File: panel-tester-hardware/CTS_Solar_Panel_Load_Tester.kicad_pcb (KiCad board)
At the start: 2 copper layers, 57 x 67.5 mm, 18 parts, among them J1 Screw_Terminal_01x02, J2 Conn_01x02_Pin, J3 Conn_01x07, J4 Conn_01x03, U1 INA219AxD, U2 YAAJ_BluePill

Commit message: Add files via upload
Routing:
- net MCU_I2C_SCL: track 67.3 -> 40.6 mm
- net MCU_I2C_SDA: track 63.3 -> 70.3 mm
- net V_SOLAR_INPUT_POS: track 80.2 -> 84.2 mm

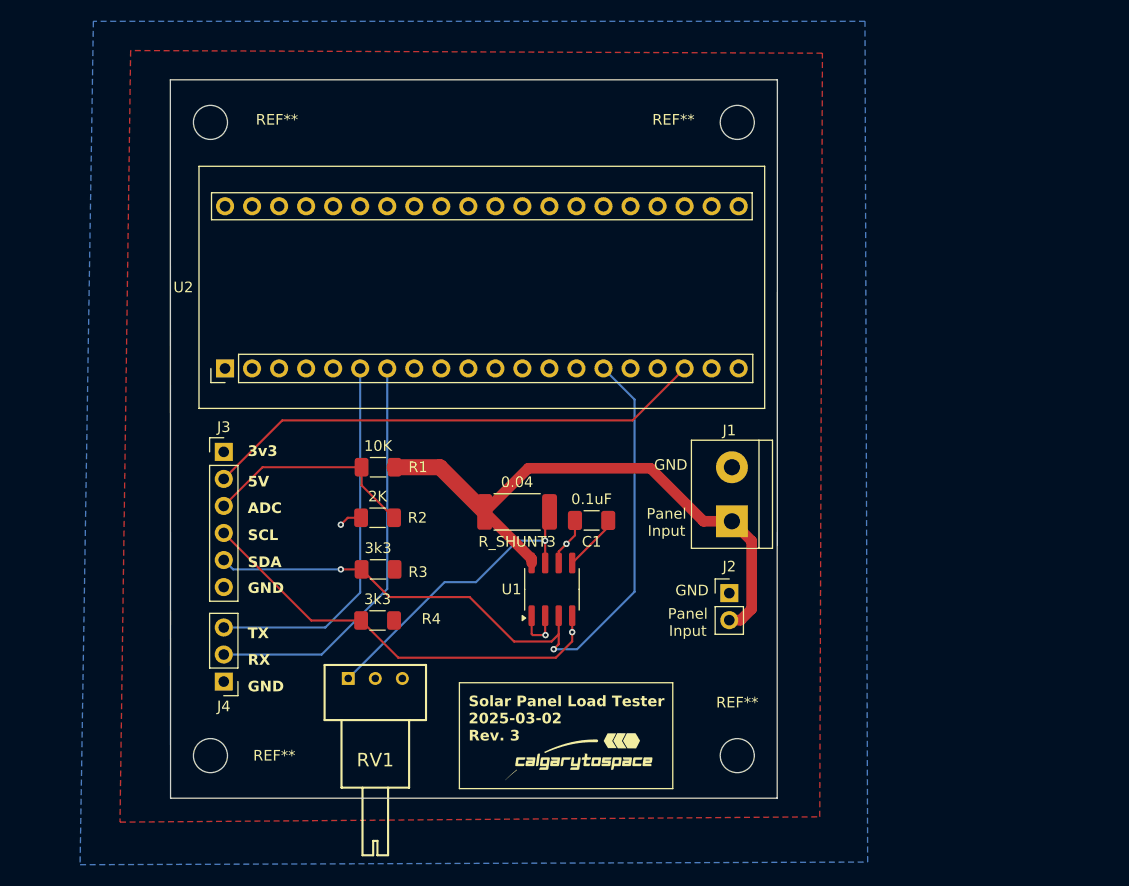
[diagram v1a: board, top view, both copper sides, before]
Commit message: made schematic for the amplifier and MOSFET
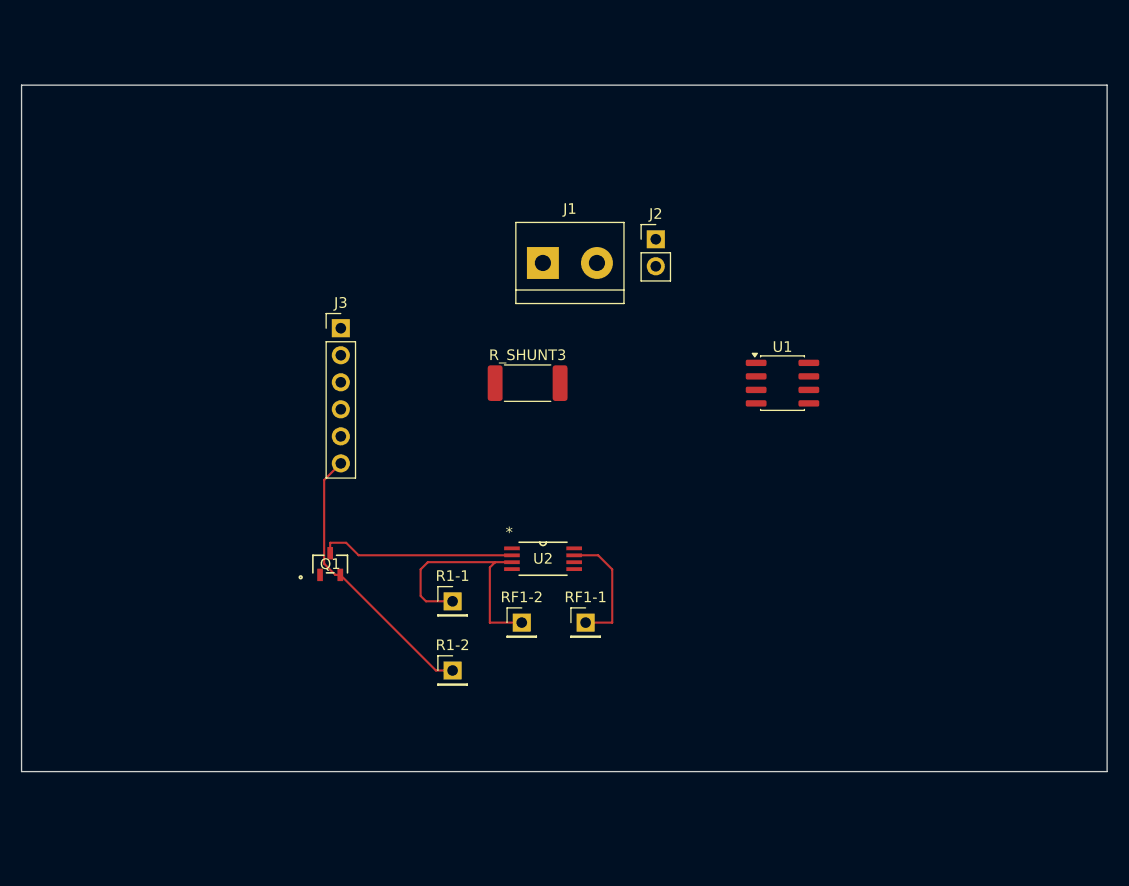
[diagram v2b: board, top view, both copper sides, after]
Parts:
- removed C1: 0.1uF, Capacitor_SMD:C_1206_3216Metric_Pad1.33x1.80mm_HandSolder
- removed G***: LOGO, LOGO
- removed J4: Conn_01x03, Connector_PinHeader_2.54mm:PinHeader_1x03_P2.54mm_Vertical
- removed R1: 10K, Resistor_SMD:R_1206_3216Metric_Pad1.30x1.75mm_HandSolder
- removed R2: 2K, Resistor_SMD:R_1206_3216Metric_Pad1.30x1.75mm_HandSolder
- removed R3, R4: 3k3, Resistor_SMD:R_1206_3216Metric_Pad1.30x1.75mm_HandSolder
- removed REF** (x4): MountingHole_3.2mm_M3, MountingHole:MountingHole_3.2mm_M3
- removed RV1: R_Potentiometer, PotentiometerCustom:3310C101102L
- added Q1: ~, mosfet:TO-236AB_SOT23_NEX, F.Cu at (107.0, 98.5)
- added R1-1: ~, Connector_PinHeader_2.54mm:PinHeader_1x01_P2.54mm_Vertical, F.Cu at (118.5, 102.0)
- added R1-2: ~, Connector_PinHeader_2.54mm:PinHeader_1x01_P2.54mm_Vertical, F.Cu at (118.5, 108.5)
- added RF1-1: ~, Connector_PinHeader_2.54mm:PinHeader_1x01_P2.54mm_Vertical, F.Cu at (131.0, 104.0)
- added RF1-2: ~, Connector_PinHeader_2.54mm:PinHeader_1x01_P2.54mm_Vertical, F.Cu at (125.0, 104.0)
- U2: value YAAJ_BluePill -> LM311PW; footprint BluePill:YAAJ_BluePill_2 -> lm311-footprints:PW8
- moved U2 34.8 mm to (127.0, 98.0), turned to 0 degrees
- moved J2 34.0 mm to (137.6, 68.0)
- moved J1 30.1 mm to (127.0, 70.2), turned to 0 degrees
- moved U1 29.1 mm to (149.5, 81.5), turned to 0 degrees
- moved J3 16.0 mm to (108.0, 76.3)
- moved R_SHUNT3 12.1 mm to (125.5, 81.5)
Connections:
- R_SHUNT3 pad 2: V_SOLAR_INPUT_POS -> Net-(U1-IN-)
- U1 pad 7: V_SOLAR_INPUT_POS -> Net-(U1-IN-)
- U2 pad 2: unconnected-(U2-PB13-Pad2) -> Net-(Q1-D)
- U2 pad 3: unconnected-(U2-PB14-Pad3) -> Net-(R1-1-Pin_1)
- U2 pad 6: Net-(J4-Pin_3) -> unconnected-(U2-BAL/STRB-Pad6)
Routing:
- net V_SOLAR_INPUT_POS: track 84.2 -> 0.00 mm, vias 1 -> 0
- net MCU_I2C_SDA: track 70.3 -> 0.00 mm, vias 2 -> 0
- net +5V: track 47.6 -> 0.00 mm
- net MCU_I2C_SCL: track 40.6 -> 0.00 mm, vias 1 -> 0
- net Net-(J4-Pin_3): track 35.2 -> 0.00 mm
- net Net-(RF1-1-Pin_1): track 38.6 -> 11.6 mm
- net Net-(R1-1-Pin_1): track 0.00 -> 23.4 mm
- net MCU_ADC_SENSE: track 20.5 -> 0.00 mm
- net Net-(Q1-D): track 0.00 -> 18.5 mm
- net GND: track 11.6 -> 26.3 mm, vias 3 -> 0
- net +3V3: track 5.40 -> 0.00 mm
- removed copper zone on F.Cu, net +3V3
- removed copper zone on B.Cu, net GND
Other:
- board size 57 x 67.5 mm -> 102 x 64.5 mm
- board text removed: "3v3"
- board text removed: "5V"
- board text removed: "ADC"
- board text removed: "GND"
- board text removed: "Panel Input"
- board text removed: "R4"
- board text removed: "RX"
- board text removed: "SCL"
- board text removed: "SDA"
- board text removed: "Solar Panel Load Tester 2025-03-02 Rev. 3"
- board text removed: "TX"

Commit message: fixed footprints and added headers
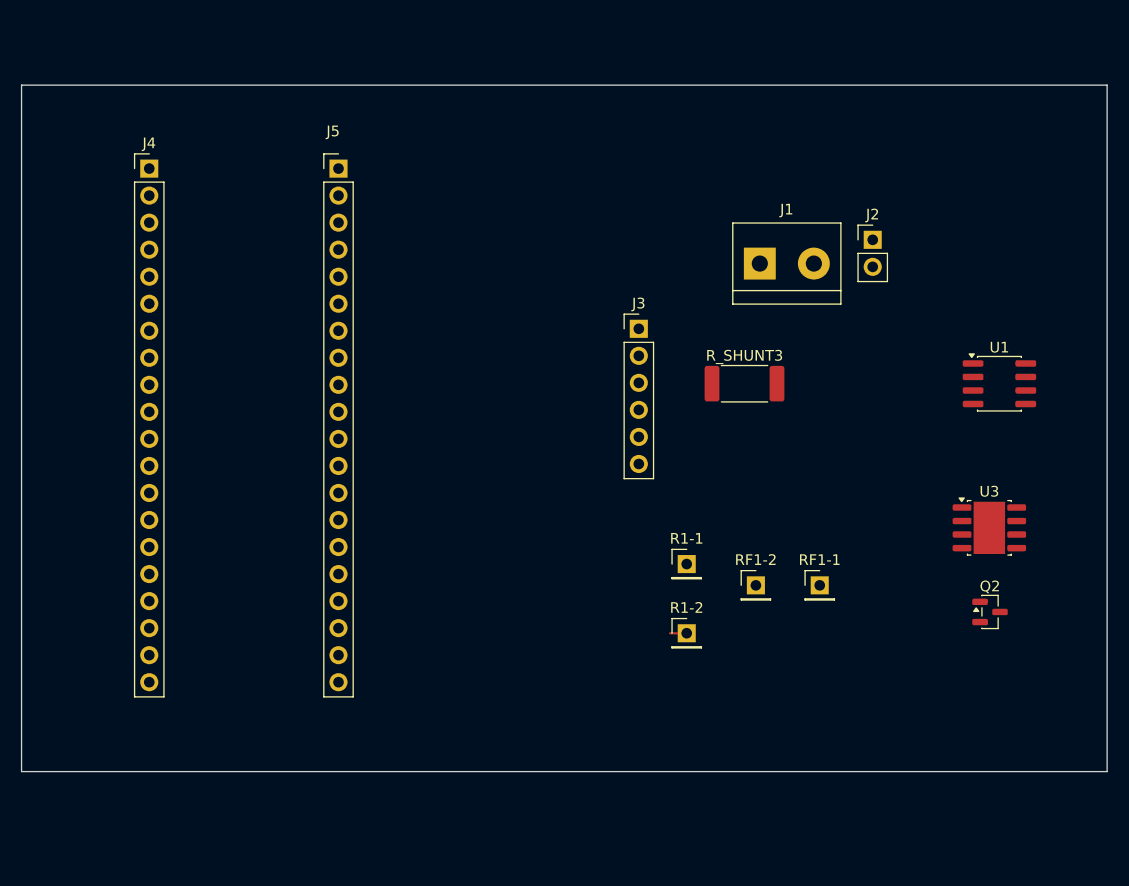
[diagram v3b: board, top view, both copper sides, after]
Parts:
- removed Q1: ~, mosfet:TO-236AB_SOT23_NEX
- removed U2: LM311PW, lm311-footprints:PW8
- added J4: Conn_01x20_Pin, Connector_PinHeader_2.54mm:PinHeader_1x20_P2.54mm_Vertical, F.Cu at (90.0, 61.3)
- added J5: Conn_01x20_Pin, Connector_PinHeader_2.54mm:PinHeader_1x20_P2.54mm_Vertical, F.Cu at (107.8, 61.3)
- added Q2: 2N7002, Package_TO_SOT_SMD:SOT-23, F.Cu at (169.0, 103.0)
- added U3: LM311, Package_SO:SOIC-8-1EP_3.9x4.9mm_P1.27mm_EP2.95x4.9mm_Mask2.71x3.4mm, F.Cu at (168.9, 95.1)
- moved J3 28.0 mm to (136.0, 76.4)
- moved R1-1 22.3 mm to (140.5, 98.5)
- moved R1-2 22.3 mm to (140.5, 105.0)
- moved RF1-1 22.3 mm to (153.0, 100.5)
- moved RF1-2 22.3 mm to (147.0, 100.5)
- moved J1 20.4 mm to (147.4, 70.3)
- moved R_SHUNT3 20.4 mm to (145.9, 81.6)
- moved J2 20.4 mm to (158.0, 68.0)
- moved U1 20.4 mm to (169.9, 81.6)
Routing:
- net GND: track 26.3 -> 1.57 mm
- net Net-(R1-1-Pin_1): track 23.4 -> 0.00 mm
- net Net-(Q1-D): track 18.5 -> 0.00 mm
- net Net-(RF1-1-Pin_1): track 11.6 -> 0.00 mm

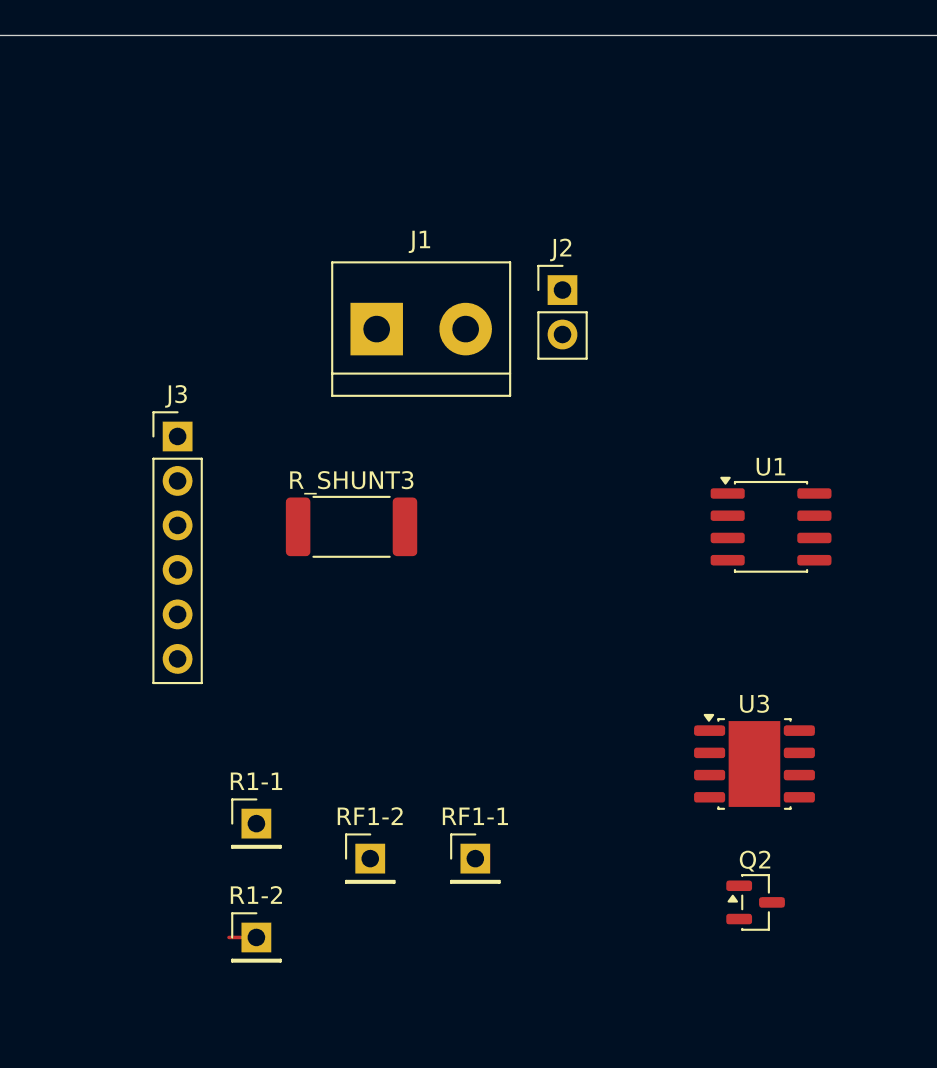
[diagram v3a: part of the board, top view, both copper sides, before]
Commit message: R2R DAC added
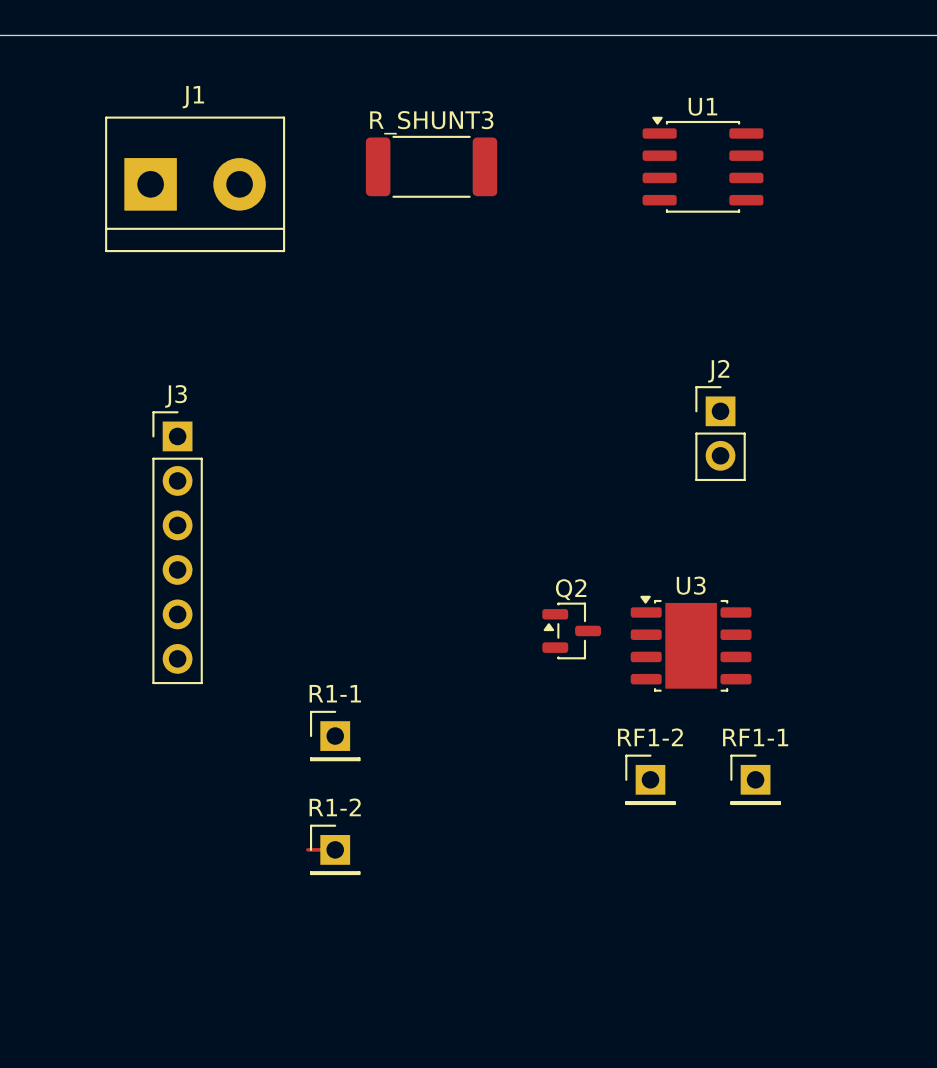
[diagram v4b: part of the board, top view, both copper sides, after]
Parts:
- moved R_SHUNT3 21.1 mm to (150.5, 61.0)
- moved U1 20.9 mm to (166.0, 61.0)
- moved Q2 18.7 mm to (158.5, 87.5)
- moved RF1-1 16.6 mm to (169.0, 96.0)
- moved RF1-2 16.6 mm to (163.0, 96.0)
- moved J1 15.3 mm to (134.5, 62.0)
- moved J2 11.4 mm to (167.0, 75.0)
- moved U3 7.65 mm to (165.3, 88.3)
- moved R1-1 6.73 mm to (145.0, 93.5)
- moved R1-2 6.73 mm to (145.0, 100.0)
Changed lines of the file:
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@@
 	(footprint "Resistor_SMD:R_2512_6332Metric_Pad1.40x3.35mm_HandSolder"
 		(layer "F.Cu")
-		(at 145.9325 81.555)
+		(at 150.5 61)
 		(descr "Resistor SMD 2512 (6332 Metric), square (rectangular) end terminal, IPC-7351 nominal with elongated pad for handsoldering. (Body size source: IPC-SM-782 page 72, https://www.pcb-3d.com/wordpress/wp-content/uploads/ipc-sm-782a_amendment_1_and_2.pdf), generated with kicad-footprint-generator")
 		(tags "resistor handsolder")
@@
 	(footprint "Package_SO:SOIC-8-1EP_3.9x4.9mm_P1.27mm_EP2.95x4.9mm_Mask2.71x3.4mm"
 		(layer "F.Cu")
-		(at 168.9375 95.095)
+		(at 165.32 88.35)
 		(descr "SOIC, 8 Pin (http://www.ti.com/lit/ds/symlink/lm5017.pdf#page=31), generated with kicad-footprint-generator ipc_gullwing_generator.py")
 		(tags "SOIC SO")
@@
 	(footprint "Connector_PinHeader_2.54mm:PinHeader_1x02_P2.54mm_Vertical"
 		(layer "F.Cu")
-		(at 157.9775 68.035)
+		(at 167 74.96)
 		(descr "Through hole straight pin header, 1x02, 2.54mm pitch, single row")
 		(tags "Through hole pin header THT 1x02 2.54mm single row")
@@
 	(footprint "Package_TO_SOT_SMD:SOT-23"
 		(layer "F.Cu")
-		(at 169 103)
+		(at 158.5 87.5)
 		(descr "SOT, 3 Pin (JEDEC TO-236 Var AB https://www.jedec.org/document_search?search_api_views_fulltext=TO-236), generated with kicad-footprint-generator ipc_gullwing_generator.py")
 		(tags "SOT TO_SOT_SMD")
@@
 	(footprint "Connector_PinHeader_2.54mm:PinHeader_1x01_P2.54mm_Vertical"
 		(layer "F.Cu")
-		(at 140.5 105)
+		(at 145 100)
 		(descr "Through hole straight pin header, 1x01, 2.54mm pitch, single row")
 		(tags "Through hole pin header THT 1x01 2.54mm single row")
@@
 	(footprint "Package_SO:SOIC-8_3.9x4.9mm_P1.27mm"
 		(layer "F.Cu")
-		(at 169.8825 81.555)
+		(at 166 61)
 		(descr "SOIC, 8 Pin (JEDEC MS-012AA, https://www.analog.com/media/en/package-pcb-resources/package/pkg_pdf/soic_narrow-r/r_8.pdf), generated with kicad-footprint-generator ipc_gullwing_generator.py")
 		(tags "SOIC SO")
@@
 		)
 		(property "Value" "INA219AxD"
-			(at 0 3.4 0)
+			(at 0 3.59 0)
 			(layer "F.Fab")
 			(effects
@@
 	(footprint "Connector_PinHeader_2.54mm:PinHeader_1x01_P2.54mm_Vertical"
 		(layer "F.Cu")
-		(at 147 100.5)
+		(at 163 96)
 		(descr "Through hole straight pin header, 1x01, 2.54mm pitch, single row")
 		(tags "Through hole pin header THT 1x01 2.54mm single row")
@@
 	(footprint "TerminalBlock:TerminalBlock_bornier-2_P5.08mm"
 		(layer "F.Cu")
-		(at 147.3675 70.265)
+		(at 134.46 62)
 		(descr "simple 2-pin terminal block, pitch 5.08mm, revamped version of bornier2")
 		(tags "terminal block bornier2")
@@
 	(footprint "Connector_PinHeader_2.54mm:PinHeader_1x01_P2.54mm_Vertical"
 		(layer "F.Cu")
-		(at 153 100.5)
+		(at 169 96)
 		(descr "Through hole straight pin header, 1x01, 2.54mm pitch, single row")
 		(tags "Through hole pin header THT 1x01 2.54mm single row")
@@
 	(footprint "Connector_PinHeader_2.54mm:PinHeader_1x01_P2.54mm_Vertical"
 		(layer "F.Cu")
-		(at 140.5 98.5)
+		(at 145 93.5)
 		(descr "Through hole straight pin header, 1x01, 2.54mm pitch, single row")
 		(tags "Through hole pin header THT 1x01 2.54mm single row")
@@
 	)
 	(segment
-		(start 140.5 105)
-		(end 138.934001 105)
+		(start 145 100)
+		(end 143.434001 100)
 		(width 0.2)
 		(layer "F.Cu")
